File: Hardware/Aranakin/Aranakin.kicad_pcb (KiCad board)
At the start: 2 copper layers, 105 x 87.8 mm, 94 parts, among them J1 5.08-2P-90, J2 Conn_01x03_Socket, J3 Conn_01x03_Socket, K1 G5LE-1, K2 G5LE-1, Q1 2N7002K, Q2 PMOS, Q3 2N7002K, Q4 2N7002K, Q5 2N7002K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

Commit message: Hardware update
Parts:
- removed C1, C3, C4, C5: 220uF, Capacitor_THT:CP_Radial_D8.0mm_P5.00mm
- removed C11: 10u, Capacitor_SMD:C_0805_2012Metric
- removed C12: 100nF, Capacitor_SMD:C_0805_2012Metric
- removed C14, C17: 100uF, Capacitor_SMD:C_Elec_6.3x7.7
- removed CC1: Conn_01x02_Socket, Connector_Molex:Molex_KK-254_AE-6410-02A_1x02_P2.54mm_Vertical
- removed D4: SS24, Diode_SMD:D_SMB
- removed J2: Conn_01x03_Socket, Connector_JST:JST_NV_B03P-NV_1x03_P5.00mm_Vertical
- removed L1: 22u, Inductor_SMD:L_APV_APH0630
- removed L3: 22n, Inductor_SMD:L_0805_2012Metric
- removed Q4: 2N7002K, Package_TO_SOT_SMD:SOT-23
- removed R10, R12, R9: 250mR 1W 1%, Resistor_SMD:R_1206_3216Metric_Pad1.30x1.75mm_HandSolder
- removed R14, R15: 10k, Resistor_SMD:R_0805_2012Metric
- added J4: 1Wire, TerminalBlock:TerminalBlock_Xinya_XY308-2.54-3P_1x03_P2.54mm_Horizontal, F.Cu at (202.1, 95.3)
- added JP2: SolderJumper_3_Open, Jumper:SolderJumper-3_P1.3mm_Open_RoundedPad1.0x1.5mm, F.Cu at (157.9, 63.7)
- added R27: 10k, Resistor_SMD:R_0805_2012Metric, F.Cu at (196.7, 96.3)
- C9: value 100n -> 100nF; footprint Capacitor_SMD:C_0402_1005Metric -> Capacitor_SMD:C_0805_2012Metric
- R21: value 1k -> 10k
- R3, R8: value 2k -> 2.2k; footprint Resistor_SMD:R_0402_1005Metric_Pad0.72x0.64mm_HandSolder -> Resistor_SMD:R_0805_2012Metric
- U7: value PC817 -> PC817XI; footprint Package_DIP:SMDIP-4_W7.62mm -> Package_DIP:DIP-4_W8.89mm_SMDSocket_LongPads
- moved H4 150.1 mm to (202.3, 60.8)
- moved U4 147.8 mm to (201.3, 137.1)
- moved D2 141.6 mm to (167.8, 69.2), turned to -90 degrees
- moved C13 141.4 mm to (175.6, 84.9), turned to -90 degrees
- moved C8 139.7 mm to (204.7, 133.7), turned to 90 degrees
- moved U3 132.7 mm to (183.1, 99.5)
- moved D1 131.6 mm to (154.5, 75.8), turned to 90 degrees
- moved PORT1 130.3 mm to (175.2, 136.8)
- moved L2 129.9 mm to (182.1, 79.7), turned to -90 degrees
- moved C15 128.2 mm to (159.8, 76.5), turned to 90 degrees
- moved D5 126.8 mm to (154.5, 94.2), turned to 90 degrees
- moved L4 119.6 mm to (168.1, 78.3), turned to 180 degrees
- moved R25 119.4 mm to (195.5, 67.2), turned to 180 degrees
- moved R24 118.8 mm to (195.4, 65.1)
- moved H3 118.5 mm to (188.3, 135.8)
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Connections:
- C9 pad 1: +3.3V -> GND
- C9 pad 2: GND -> +3.3V
- D13 pad 1: Vin -> Net-(D13-K)
- J3 pad 2: ADC0 -> ADC
- PWM1 pad 2: Vin -> Net-(D13-K)
- R11 pad 2: ADC0 -> ADC
- R13 pad 2: ADC0 -> ADC
- R21 pad 1: relayPWR -> Net-(D8-A)
- R21 pad 2: Net-(D8-A) -> relayPWR
- R3 pad 1: Net-(D3-K) -> Net-(D1-A)
- R3 pad 2: Net-(D1-A) -> Net-(D3-K)
- R8 pad 1: Net-(D6-K) -> Net-(D5-A)
- R8 pad 2: Net-(D5-A) -> Net-(D6-K)
- U5 pad 1: CC_CH0 -> 1Wire
- U5 pad 10: LED_PIN -> RELAY1_PIN
- U5 pad 12: RELAY1_PIN -> Opto
- U5 pad 13: RELAY0_PIN -> ADC
- U5 pad 3: Opto -> SDA
- U5 pad 4: SDA -> SCL
- U5 pad 5: SCL -> unconnected-(U5-GPIO9-Pad5)
- U5 pad 6: unconnected-(U5-GPIO10-Pad6) -> LED_PIN
- U5 pad 9: ADC0 -> RELAY0_PIN
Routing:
- net +5V: track 0.00 -> 210.1 mm, vias 0 -> 3
- net +3.3V: track 0.00 -> 199.4 mm, vias 0 -> 4
- net GND: track 0.00 -> 149.4 mm, vias 0 -> 220
- net relayPWR: track 0.00 -> 119.4 mm, vias 0 -> 5
- net openDrain: track 0.00 -> 106.5 mm, vias 0 -> 1
- net 1Wire: track 0.00 -> 79.7 mm
- net SCL: track 0.00 -> 65.5 mm, vias 0 -> 2
- net SDA: track 0.00 -> 59.9 mm, vias 0 -> 3
- net Net-(RL2-Pin_2): track 0.00 -> 53.8 mm
- net Net-(RL1-Pin_2): track 0.00 -> 53.3 mm
- net 12V_enable: track 0.00 -> 45.1 mm, vias 0 -> 2
- net VCC: track 0.00 -> 41.9 mm
- net Vin: track 0.00 -> 39.5 mm
- net Net-(D1-A): track 0.00 -> 34.3 mm
- net ADC: track 0.00 -> 32.2 mm
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- added copper zone on B.Cu, net GND
- added copper zone on F.Cu, net GND
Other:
- board size 105 x 87.8 mm -> 90 x 85 mm
- board text added: "+"
- board text added: "+VIN-"
- board text added: "-"
- board text added: "5V"
- board text added: "GND IO4 3V3"

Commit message: Added first layout and fabrication files
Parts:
- added PORT2: Conn_01x03_Socket, Connector_PinHeader_2.54mm:PinHeader_1x03_P2.54mm_Vertical, F.Cu at (170.3, 120.9)
- moved R26 0.82 mm to (170.6, 124.2)
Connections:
- U5 pad 7: unconnected-(U5-GPIO20/U0RXD-Pad7) -> Net-(PORT2-Pin_1)
- U5 pad 8: unconnected-(U5-GPIO21/U0TXD-Pad8) -> Net-(PORT2-Pin_2)
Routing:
- net Net-(PORT2-Pin_2): track 0.00 -> 3.37 mm
- net Net-(PORT2-Pin_1): track 0.00 -> 3.37 mm
- net LED_PIN: track 2.56 -> 3.09 mm
- net GND: vias 220 -> 218

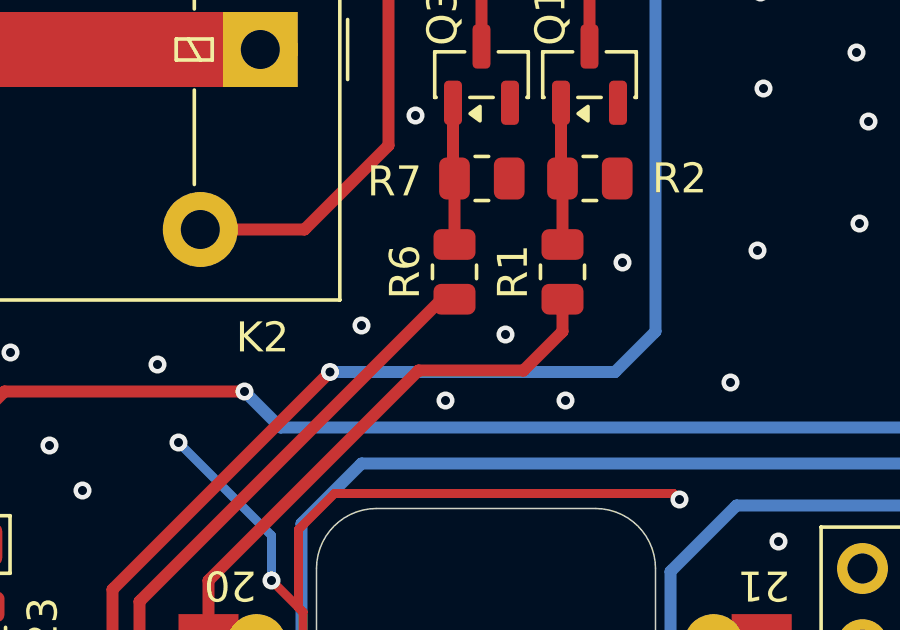
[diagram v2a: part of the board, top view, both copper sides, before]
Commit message: Fabrication files update
Removed copper fill on antenna zone.
In future versions, put relay far away from ESP.

Move fast and break things
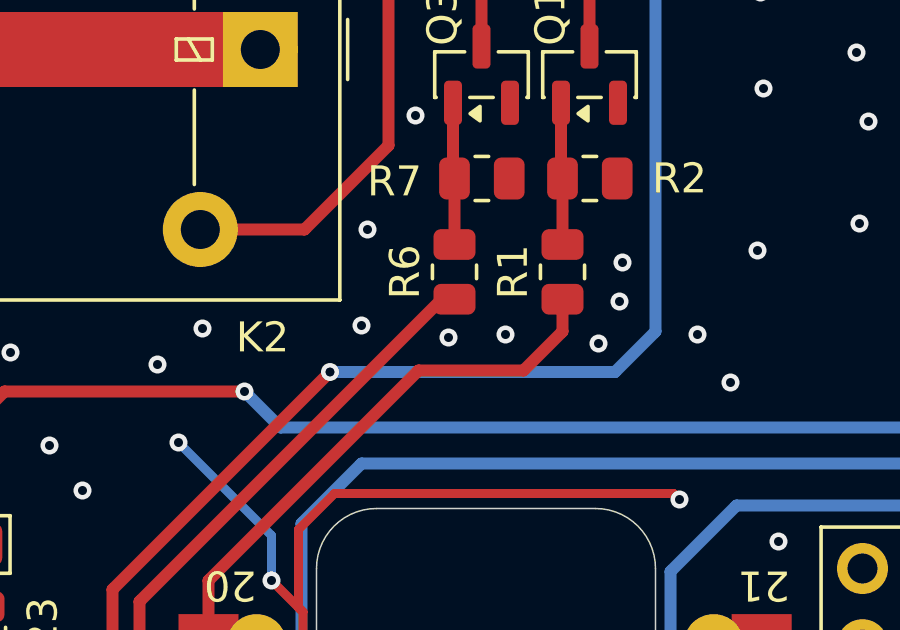
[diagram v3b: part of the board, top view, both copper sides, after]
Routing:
- net GND: vias 218 -> 222
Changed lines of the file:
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@@
 	)
 	(via
+		(at 162.2 106.9)
+		(size 0.6)
+		(drill 0.3)
+		(layers "F.Cu" "B.Cu")
+		(free yes)
+		(net 1)
+	)
+	(via
 		(at 184.8 84.5)
 		(size 0.6)
@@
 	)
 	(via
+		(at 153.8 104.5)
+		(size 0.6)
+		(drill 0.3)
+		(layers "F.Cu" "B.Cu")
+		(free yes)
+		(net 1)
+	)
+	(via
 		(at 175.1 75.5)
 		(size 0.6)
@@
 	)
 	(via
-		(at 156.4 110.2)
-		(size 0.6)
-		(drill 0.3)
-		(layers "F.Cu" "B.Cu")
-		(free yes)
-		(net 1)
-	)
-	(via
 		(at 189.1 92)
 		(size 0.6)
@@
 	)
 	(via
+		(at 156.5 108.1)
+		(size 0.6)
+		(drill 0.3)
+		(layers "F.Cu" "B.Cu")
+		(free yes)
+		(net 1)
+	)
+	(via
 		(at 135.9 109.2)
 		(size 0.6)
@@
 	)
 	(via
+		(at 148.3 107.8)
+		(size 0.6)
+		(drill 0.3)
+		(layers "F.Cu" "B.Cu")
+		(free yes)
+		(net 1)
+	)
+	(via
 		(at 175.7 71.6)
 		(size 0.6)
@@
 	)
 	(via
-		(at 160.4 110.2)
-		(size 0.6)
-		(drill 0.3)
-		(layers "F.Cu" "B.Cu")
-		(free yes)
-		(net 1)
-	)
-	(via
 		(at 182.4 108.5)
 		(size 0.6)
@@
 	)
 	(via
+		(at 161.5 108.3)
+		(size 0.6)
+		(drill 0.3)
+		(layers "F.Cu" "B.Cu")
+		(free yes)
+		(net 1)
+	)
+	(via
 		(at 154.5 75.8)
 		(size 0.6)
@@
 	)
 	(via
+		(at 164.8 108)
+		(size 0.6)
+		(drill 0.3)
+		(layers "F.Cu" "B.Cu")
+		(free yes)
+		(net 1)
+	)
+	(via
 		(at 186.6 88.9)
 		(size 0.6)
@@
 			)
 		)
+	)
+	(zone
+		(net 0)
+		(net_name "")
+		(layers "F.Cu" "B.Cu")
+		(hatch edge 0.5)
+		(connect_pads
+			(clearance 0)
+		)
+		(min_thickness 0.25)
+		(filled_areas_thickness no)
+		(keepout
+			(tracks allowed)
+			(vias allowed)
+			(pads allowed)
+			(copperpour not_allowed)
+			(footprints allowed)
+		)
+		(placement
+			(enabled no)
+			(sheetname "")
+		)
+		(fill
+			(thermal_gap 0.5)
+			(thermal_bridge_width 0.5)
+		)
+		(polygon
+			(pts
+				(xy 152.595232 116.3) (xy 150.895232 114.4) (xy 150.895232 108.8) (xy 164.395232 108.8) (xy 164.395232 114.5)
+				(xy 162.895232 116.3)
+			)
+		)
